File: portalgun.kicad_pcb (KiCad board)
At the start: 4 copper layers, 125.5 x 52.3 mm, 63 parts, among them J1 Conn_01x02_Male, J2 Rotary Encoder / Switch Header, J3 Conn_01x02_Male, J4 Conn_01x02_Male, J5 Conn_02x03_Odd_Even, J6 AVR-ISP-6, J7 Conn_01x04_Male, J8 Conn_01x04_Male, Q1 MMBT3904, Q2 MMBT3904, Q3 MMBT3904, Q4 MMBT3904, Q5 MMBT3904, U1 NCP1421, U2 LM358, U3 NCP4589DSN33T1G, U4 STM32L011G4Ux, U5 SC56-11GWA, U6 SC56-11GWA, U7 ATmega48P-20MMHR, U8 SC56-11GWA, U9 SC56-11GWA

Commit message: Main Board Rev A files
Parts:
- removed C12, C14: 1uF, Capacitor_SMD:C_0603_1608Metric
- removed J6: AVR-ISP-6, Connector_PinHeader_2.54mm:PinHeader_2x03_P2.54mm_Vertical
- removed J7, J8: Conn_01x04_Male, Connector_PinHeader_2.00mm:PinHeader_1x04_P2.00mm_Vertical
- removed Q4, Q5: MMBT3904, Package_TO_SOT_SMD:SOT-23
- removed R12, R31, R32, R33, R34: 100, Resistor_SMD:R_0603_1608Metric_Pad0.98x0.95mm_HandSolder
- removed R19, R20, R29, R30: 1k, Resistor_SMD:R_0603_1608Metric
- removed R21, R22, R23, R24, R25, R26, R27, R28: 220, Resistor_SMD:R_0603_1608Metric
- removed R7: 10k, Resistor_SMD:R_0603_1608Metric_Pad0.98x0.95mm_HandSolder
- removed U9: SC56-11GWA, Display_Kingbright:SC56-11GWA
- added C3: 1uF, Capacitor_SMD:C_0603_1608Metric, F.Cu at (203.2, 98.0)
- added C4: 100nF, Capacitor_SMD:C_0603_1608Metric, F.Cu at (201.7, 98.0)
- added C9: 1uF, Capacitor_SMD:C_0603_1608Metric, F.Cu at (216.2, 97.5)
- added J10: Conn_01x02_Male, Connector_PinHeader_2.00mm:PinHeader_1x02_P2.00mm_Vertical, F.Cu at (186.5, 116.0)
- added J9: Conn_01x04_Female, Connector_Molex:Molex_PicoBlade_53047-0410_1x04_P1.25mm_Vertical, F.Cu at (209.0, 95.0)
- added R15: 10k, Resistor_SMD:R_0603_1608Metric, F.Cu at (207.8, 100.8)
- added R16: 10k, Resistor_SMD:R_0603_1608Metric, F.Cu at (207.8, 103.9)
- added SW1: SW_MEC_5E, Button_Switch_THT:SW_TH_Tactile_Omron_B3F-10xx, F.Cu at (210.1, 116.1)
- added SW2: SW_MEC_5E, Button_Switch_THT:SW_TH_Tactile_Omron_B3F-10xx, F.Cu at (210.1, 106.2)
- C10, C8: value 10uF -> 1uF; footprint Capacitor_Tantalum_SMD:CP_EIA-2012-15_AVX-P -> Capacitor_SMD:C_0603_1608Metric
- C2: value 1uF -> 10uF; footprint Capacitor_SMD:C_0603_1608Metric -> Capacitor_SMD:C_0805_2012Metric; moved to F.Cu
- J2: value Rotary Encoder / Switch Header -> Conn_01x07_Male; footprint Connector_PinHeader_2.00mm:PinHeader_1x05_P2.00mm_Vertical -> Connector_Molex:Molex_PicoBlade_53047-0710_1x07_P1.25mm_Vertical
- J5: value Conn_02x03_Odd_Even -> Conn_01x02_Male; footprint Connector_PinHeader_2.54mm:PinHeader_1x06_P2.54mm_Horizontal -> Connector_PinHeader_2.00mm:PinHeader_1x02_P2.00mm_Vertical
- Q1: value MMBT3904 -> BS316N
- Q2, Q3: value MMBT3904 -> BS316N; moved to F.Cu
- R10, R11: value 100 -> 200; footprint Resistor_SMD:R_0603_1608Metric_Pad0.98x0.95mm_HandSolder -> Resistor_SMD:R_0603_1608Metric
- R5: value 10k -> 1k; footprint Resistor_SMD:R_0603_1608Metric_Pad0.98x0.95mm_HandSolder -> Resistor_SMD:R_0603_1608Metric
- R6: footprint Resistor_SMD:R_0603_1608Metric_Pad0.98x0.95mm_HandSolder -> Resistor_SMD:R_0603_1608Metric
- R8: value 1k -> 200; footprint Resistor_SMD:R_0603_1608Metric_Pad0.98x0.95mm_HandSolder -> Resistor_SMD:R_0603_1608Metric
- R9: value 100 -> 10k; footprint Resistor_SMD:R_0603_1608Metric_Pad0.98x0.95mm_HandSolder -> Resistor_SMD:R_0603_1608Metric
- U2: value LM358 -> ESP-12F; footprint Package_SO:SSOP-8_3.95x5.21x3.27mm_P1.27mm -> RF_Module:ESP-12E
- U3: value NCP4589DSN33T1G -> MIC5504-3.3YM5
- U4: value STM32L011G4Ux -> SGTL5000XNLA3; footprint Package_DFN_QFN:QFN-28_4x4mm_P0.5mm -> Package_DFN_QFN:QFN-20-1EP_3x3mm_P0.4mm_EP1.65x1.65mm
- U5: value SC56-11GWA -> MIC5504-1.8YM5; footprint Display_Kingbright:SC56-11GWA -> Package_TO_SOT_SMD:SOT-23-5
- U6, U8: value SC56-11GWA -> 74AHC1G125; footprint Display_Kingbright:SC56-11GWA -> Package_TO_SOT_SMD:SOT-353_SC-70-5
- U7: value ATmega48P-20MMHR -> 74AHC1G125; footprint Package_DFN_QFN:QFN-28-1EP_4x4mm_P0.45mm_EP2.4x2.4mm -> Package_TO_SOT_SMD:SOT-353_SC-70-5; moved to F.Cu
- moved U2 179.2 mm to (234.8, 112.9), turned to 180 degrees
- moved C11 176.7 mm to (239.8, 96.5), turned to 90 degrees
- moved C10 149.3 mm to (204.0, 106.7), turned to 270 degrees
- moved J4 140.8 mm to (204.5, 94.2), turned to 270 degrees
- moved C2 110.6 mm to (241.8, 96.5), turned to 90 degrees
- moved U8 103.7 mm to (223.8, 101.1), turned to 270 degrees
- moved U6 96.9 mm to (217.7, 101.1)
- moved U7 93.6 mm to (220.7, 101.1), turned to 90 degrees
- moved U5 82.7 mm to (201.2, 106.9), turned to 0 degrees
- moved Q3 69.4 mm to (199.8, 112.5)
- moved Q2 65.7 mm to (191.3, 112.5), turned to 270 degrees
- moved C1 54.8 mm to (185.2, 97.0), turned to 180 degrees
- moved J1 52.8 mm to (186.2, 94.2), turned to 270 degrees
- moved C7 47.1 mm to (187.5, 109.5), turned to 180 degrees
- moved L1 46.5 mm to (189.2, 98.6), turned to 270 degrees
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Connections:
- net Net-(U4-Pad4) renamed /Audio DAC/HP_L
- C10 pad 1: Net-(C10-Pad1) -> +1V8
- C10 pad 2: Net-(C10-Pad2) -> GND
- C11 pad 1: Net-(C11-Pad1) -> +3V3
- C11 pad 2: Net-(C11-Pad2) -> GND
- C2 pad 1: VBAT -> +3V3
- C8 pad 1: VBAT -> +3V3
- J2 pad 1: SWITCH -> +5V
- J2 pad 2: +3V3 -> GND
- J2 pad 3: ENCODER_B -> Net-(J2-Pad3)
- J2 pad 4: +3V3 -> Net-(J2-Pad4)
- J2 pad 5: ENCODER_A -> Net-(J2-Pad5)
- J3 pad 1: VBAT -> Net-(J3-Pad1)
- J4 pad 1: Net-(C11-Pad2) -> /Audio DAC/AOUT+
- J4 pad 2: GND -> /Audio DAC/AOUT-
- J5 pad 1: +3V3 -> Net-(J5-Pad1)
- Q1 pad 1: Net-(Q1-Pad1) -> LED1
- Q1 pad 3: Net-(J3-Pad2) -> Net-(J10-Pad2)
- Q2 pad 1: Net-(Q2-Pad1) -> LED2
- Q2 pad 3: Net-(Q2-Pad3) -> Net-(J5-Pad2)
- Q3 pad 1: Net-(Q3-Pad1) -> LED3
- Q3 pad 3: Net-(Q3-Pad3) -> Net-(J3-Pad2)
- R10 pad 1: Net-(J5-Pad3) -> Net-(J5-Pad1)
- R10 pad 2: LPUART1_TX -> +5V
- R11 pad 1: SYS_SWCLK -> Net-(J10-Pad1)
- R11 pad 2: Net-(J5-Pad4) -> +5V
- R5 pad 1: ENCODER_A -> Net-(J2-Pad5)
- R5 pad 2: GND -> Net-(R5-Pad2)
- R6 pad 1: ENCODER_B -> /bootsel
- R6 pad 2: GND -> +3V3
- R8 pad 1: LED_GATE -> Net-(J3-Pad1)
- R8 pad 2: Net-(Q1-Pad1) -> +5V
- R9 pad 1: SYS_SWDIO -> +3V3
- R9 pad 2: Net-(J5-Pad2) -> /~rst
- U2 pad 1: Net-(C11-Pad1) -> /~rst
- U2 pad 2: Net-(C11-Pad1) -> Net-(U2-Pad2)
- U2 pad 3: Net-(C10-Pad2) -> +3V3
- U2 pad 4: (no net) -> Net-(U2-Pad4)
- U2 pad 5: (no net) -> LED3
- U2 pad 6: (no net) -> LED2
- U2 pad 7: (no net) -> LED1
- U2 pad 8: (no net) -> +3V3
- U3 pad 4: +5V -> Net-(U3-Pad4)
- U4 pad 1: Net-(U4-Pad1) -> /Audio DAC/AOUT+
- U4 pad 11: SPI1_SCK -> Net-(U4-Pad11)
- U4 pad 12: SPI1_MISO -> +1V8
- U4 pad 13: SPI1_MOSI -> /Audio DAC/SYS_MCLK
- U4 pad 14: Net-(U4-Pad14) -> I2S_LRCLK
- U4 pad 15: Net-(U4-Pad15) -> I2S_BCLK
- U4 pad 16: GND -> /Audio DAC/I2S_DOUT
- U4 pad 17: +3V3 -> ESP_RXD
- U4 pad 18: SPI1_NSS -> SDA
- U4 pad 19: I2C1_SCL -> SCL
- U4 pad 2: Net-(U4-Pad2) -> /Audio DAC/AOUT-
- U4 pad 20: I2C1_SDA -> +3V3
- U4 pad 21: SYS_SWDIO -> GND
- U4 pad 3: Net-(U4-Pad3) -> +3V3
- U4 pad 5: +3V3 -> /Audio DAC/VAG
- U4 pad 6: LPUART1_RX -> Net-(U4-Pad6)
- U4 pad 7: LPUART1_TX -> Net-(U4-Pad7)
- U5 pad 1: /7 Segment Display/segment_g -> +3V3
- U5 pad 2: /7 Segment Display/segment_f -> GND
- U5 pad 3: Net-(U5-Pad3) -> +3V3
- U5 pad 4: /7 Segment Display/segment_a -> Net-(U5-Pad4)
- U5 pad 5: /7 Segment Display/segment_b -> +1V8
- U6 pad 1: /7 Segment Display/segment_g -> GND
- U6 pad 2: /7 Segment Display/segment_f -> SPI1_SCK
- U6 pad 3: Net-(U6-Pad3) -> GND
- U6 pad 4: /7 Segment Display/segment_a -> Net-(J2-Pad3)
- U6 pad 5: /7 Segment Display/segment_b -> +5V
- U7 pad 1: Net-(R24-Pad1) -> GND
- U7 pad 2: Net-(R25-Pad1) -> SPI1_MOSI
- U7 pad 3: VBAT -> GND
- U7 pad 4: GND -> Net-(J2-Pad4)
- U7 pad 5: Net-(U7-Pad5) -> +5V
- U8 pad 1: /7 Segment Display/segment_g -> GND
- U8 pad 2: /7 Segment Display/segment_f -> Net-(R5-Pad2)
- U8 pad 3: Net-(U8-Pad3) -> GND
- U8 pad 4: /7 Segment Display/segment_a -> SPI1_MISO
- U8 pad 5: /7 Segment Display/segment_b -> +5V
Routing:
- net LED1: track 0.00 -> 61.5 mm, vias 0 -> 2
- net /7 Segment Display/segment_g: track 56.9 -> 0.00 mm, vias 1 -> 0
- net /7 Segment Display/segment_b: track 55.0 -> 0.00 mm, vias 3 -> 0
- net LED2: track 0.00 -> 53.6 mm, vias 0 -> 2
- net /7 Segment Display/segment_f: track 53.5 -> 0.00 mm, vias 2 -> 0
- net /7 Segment Display/segment_e: track 51.3 -> 0.00 mm
- net /7 Segment Display/segment_a: track 48.3 -> 0.00 mm, vias 2 -> 0
- net /7 Segment Display/segment_c: track 48.1 -> 0.00 mm
- net +5V: track 12.2 -> 59.5 mm, vias 0 -> 11
- net /7 Segment Display/segment_d: track 45.6 -> 0.00 mm
- net /~rst: track 0.00 -> 45.6 mm
- net LED3: track 0.00 -> 45.2 mm, vias 0 -> 2
- net /7 Segment Display/decimal_point: track 45.2 -> 0.00 mm
- net ESP_RXD: track 0.00 -> 36.9 mm, vias 0 -> 1
- net SCL: track 0.00 -> 32.0 mm
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- added copper zone on In2.Cu, net +5V
- added copper zone on In2.Cu, net VBAT
- removed copper zone on In2.Cu, net GND
- removed copper zone on In1.Cu, net VBAT
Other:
- board size 125.5 x 52.3 mm -> 61.5 x 25 mm
- net class Default: clearance 0.2032 -> 0.1524
- rule trace_clearance: 0.2032 -> 0.1524
- rule via_min_size: 0.4 -> 0.6
- board text added: "3V"
- board text added: "G"
- board text added: "GND"
- board text added: "MISO"
- board text added: "MOSI"
- board text added: "Portal Gun Main Board rev A"
- board text added: "RX"
- board text added: "SCK"
- board text added: "TX"
- board text added: "~RST"
- board text added: "~SS"
- board text removed: "Display TODO - Power and Ground traces - Decoupling caps - SPI header"
- board text removed: "Stackup 1 (F.Cu): Signal + ground pour 2 (In1.Cu): Ground plane 3: (In2. Cu): Power plane 4: (B.Cu): Signal + ground pour"

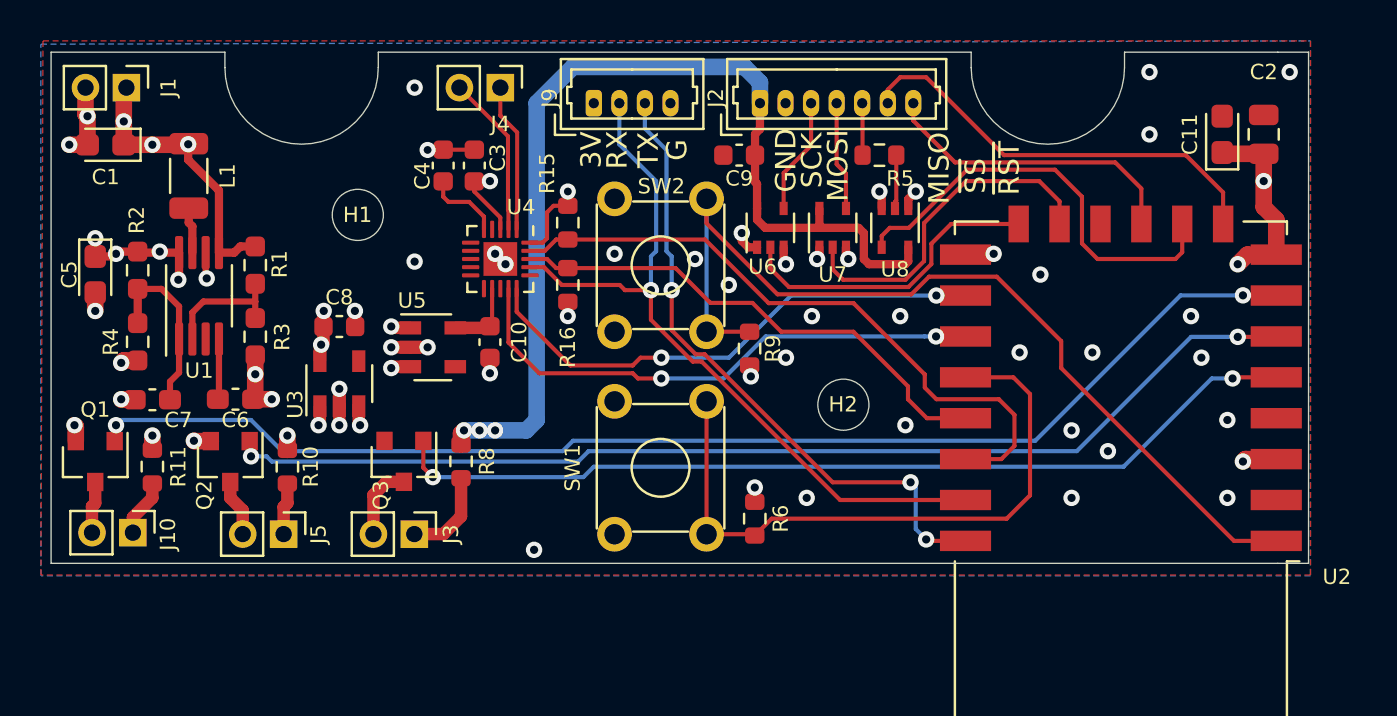
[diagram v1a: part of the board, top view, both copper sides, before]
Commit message: Rev B Portal Gun Mainboard as ordered
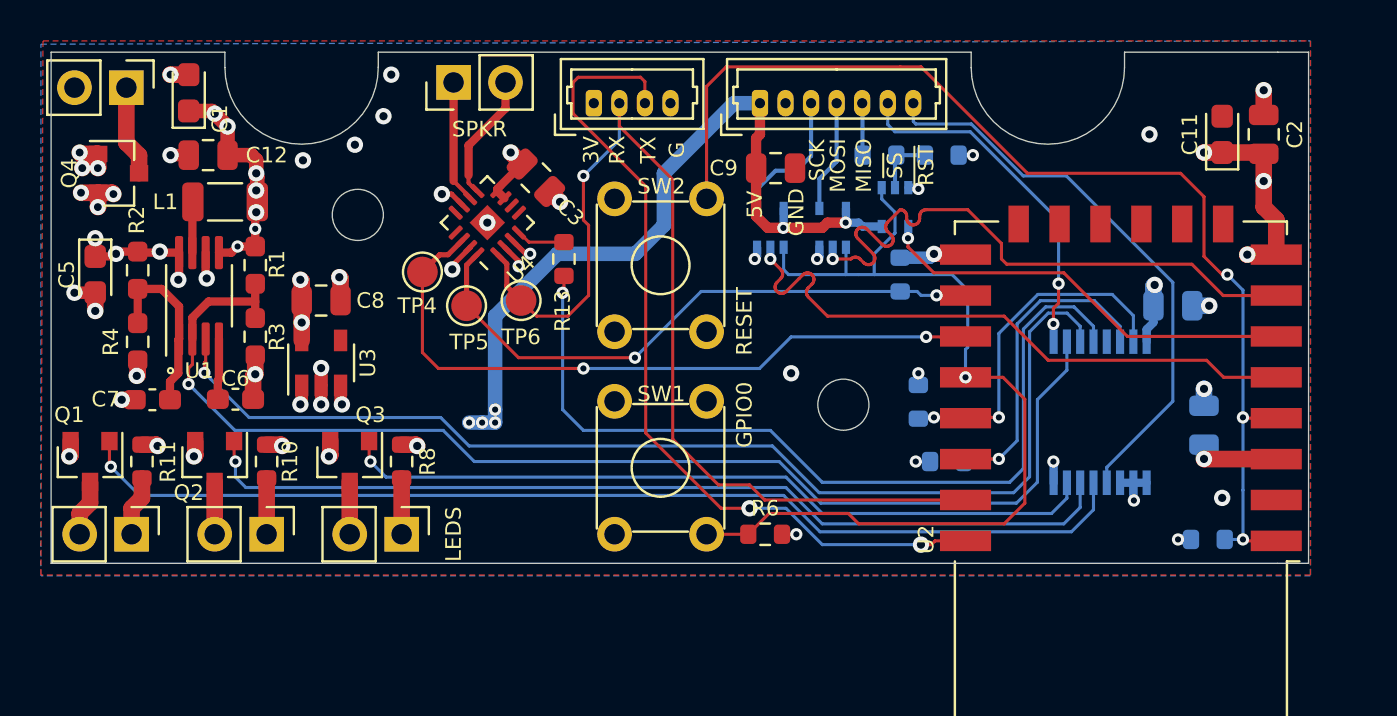
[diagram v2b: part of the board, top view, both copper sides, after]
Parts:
- removed C10: 1uF, Capacitor_SMD:C_0603_1608Metric
- removed C4: 100nF, Capacitor_SMD:C_0603_1608Metric
- removed U5: MIC5504-1.8YM5, Package_TO_SOT_SMD:SOT-23-5
- added C12: 1uF, Capacitor_SMD:C_0805_2012Metric, F.Cu at (190.2, 97.5)
- added C13: 1uF, Capacitor_SMD:C_0805_2012Metric, B.Cu at (238.9, 110.7)
- added C14: 1uF, Capacitor_SMD:C_0805_2012Metric, B.Cu at (237.4, 104.9)
- added Q4: Q_PMOS_DGS, Package_TO_SOT_SMD:SOT-23, F.Cu at (185.8, 98.4)
- added R12: 10k, Resistor_SMD:R_0603_1608Metric, B.Cu at (226.1, 97.5)
- added R13: 634kR, Resistor_SMD:R_0603_1608Metric, F.Cu at (207.6, 102.6)
- added R7: 10k, Resistor_SMD:R_0603_1608Metric, B.Cu at (224.0, 103.4)
- added TP4: I2S_LRCIN_TP, TestPoint:TestPoint_Pad_D1.5mm, F.Cu at (200.7, 103.3)
- added TP5: I2S_BCLK_TP, TestPoint:TestPoint_Pad_D1.5mm, F.Cu at (202.8, 104.9)
- added TP6: I2S_DIN_TP, TestPoint:TestPoint_Pad_D1.5mm, F.Cu at (205.5, 104.6)
- added U9: PCA9534, Package_SO:SSOP-16_5.3x6.2mm_P0.65mm, B.Cu at (233.8, 110.1)
- C2: value 10uF -> 1uF
- C3, C8, C9: footprint Capacitor_SMD:C_0603_1608Metric -> Capacitor_SMD:C_0805_2012Metric
- J1, J10, J3, J4, J5: footprint Connector_PinHeader_2.00mm:PinHeader_1x02_P2.00mm_Vertical -> Connector_PinHeader_2.54mm:PinHeader_1x02_P2.54mm_Vertical
- R15, R16, R5, R9, U6, U7, U8: moved to B.Cu
- U4: value SGTL5000XNLA3 -> MAX98357AETE; footprint Package_DFN_QFN:QFN-20-1EP_3x3mm_P0.4mm_EP1.65x1.65mm -> Package_DFN_QFN:TQFN-16-1EP_3x3mm_P0.5mm_EP1.23x1.23mm
- moved R9 24.3 mm to (239.1, 116.3), turned to 0 degrees
- moved R15 21.9 mm to (226.3, 112.5), turned to 0 degrees
- moved R16 18.1 mm to (224.9, 109.6), turned to 90 degrees
- moved C1 4.79 mm to (189.2, 94.5), turned to 90 degrees
- moved C3 3.07 mm to (206.2, 98.6), turned to 315 degrees
- moved R8 2.91 mm to (199.6, 112.5)
- moved Q3 2.65 mm to (197.1, 112.5)
- moved J4 2.30 mm to (202.2, 94.0), turned to 90 degrees
- moved L1 2.18 mm to (191.0, 99.8), turned to 180 degrees
- moved U4 1.89 mm to (203.8, 100.8), turned to 135 degrees
- moved C9 1.89 mm to (217.9, 98.2), turned to 0 degrees
- moved C8 1.55 mm to (195.7, 104.6)
- moved U3 1.35 mm to (195.7, 107.7)
- moved R10 1.05 mm to (193.0, 112.5)
- moved U8 1.02 mm to (223.8, 100.1)
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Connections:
- net /Audio DAC/SYS_MCLK renamed Net-(U4-Pad13)
- net LBI_EN renamed NCP_LBI_EN
- net Net-(J2-Pad3) renamed /EXT_SCK
- net Net-(J2-Pad4) renamed /EXT_MOSI
- net Net-(J2-Pad5) renamed /EXT_MISO
- J1 pad 1: VBAT -> /bat+
- J2 pad 6: SPI1_NSS -> ~SPI1_SS
- R6 pad 1: /bootsel -> ~BUFFER_EN
- SW1 pad 3: /bootsel -> ~BUFFER_EN
- SW1 pad 4: /bootsel -> Net-(SW1-Pad4)
- SW2 pad 3: /~rst -> Net-(SW2-Pad3)
- U1 pad 3: LBO -> NCP_LBO
- U2 pad 10: SPI1_MISO -> Net-(U2-Pad10)
- U2 pad 11: ~DISPLAY_RST -> Net-(U2-Pad11)
- U2 pad 13: SPI1_MOSI -> Net-(U2-Pad13)
- U2 pad 14: SPI1_SCK -> Net-(U2-Pad14)
- U2 pad 18: /bootsel -> ~BUFFER_EN
- U2 pad 4: Net-(U2-Pad4) -> /~rst
- U2 pad 5: LED3 -> SPI1_SCK
- U2 pad 6: LED2 -> SPI1_MISO
- U2 pad 7: LED1 -> SPI1_MOSI
- U2 pad 9: SPI1_NSS -> Net-(U2-Pad9)
- U4 pad 1: /Audio DAC/AOUT+ -> ESP_RXD
- U4 pad 10: Net-(U4-Pad10) -> /Audio DAC/AOUT+
- U4 pad 11: Net-(U4-Pad11) -> GND
- U4 pad 12: +1V8 -> Net-(U4-Pad12)
- U4 pad 15: I2S_BCLK -> GND
- U4 pad 16: /Audio DAC/I2S_DOUT -> I2S_BCLK
- U4 pad 17: ESP_RXD -> GND
- U4 pad 2: /Audio DAC/AOUT- -> +3V3
- U4 pad 3: +3V3 -> GND
- U4 pad 4: /Audio DAC/HP_L -> /Audio DAC/~SD_MODE
- U4 pad 5: /Audio DAC/VAG -> Net-(U4-Pad5)
- U4 pad 7: Net-(U4-Pad7) -> +3V3
- U4 pad 8: Net-(U4-Pad8) -> +3V3
- U4 pad 9: Net-(U4-Pad9) -> /Audio DAC/AOUT-
- U6 pad 1: GND -> ~BUFFER_EN
- U7 pad 1: GND -> ~BUFFER_EN
- U8 pad 1: GND -> ~BUFFER_EN
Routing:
- net NCP_LBO: track 0.00 -> 55.8 mm, vias 0 -> 1
- net NCP_LBI_EN: track 6.27 -> 61.9 mm, vias 0 -> 1
- net ~BUFFER_EN: track 0.00 -> 46.1 mm, vias 0 -> 1
- net /Audio DAC/~SHUTDOWN: track 0.00 -> 42.7 mm, vias 0 -> 1
- net /bootsel: track 31.6 -> 0.00 mm
- net SPI1_NSS: track 21.2 -> 0.00 mm
- net ~SPI1_SS: track 0.00 -> 17.4 mm, vias 0 -> 2
- net SPI1_SCK: track 15.4 -> 30.5 mm, vias 0 -> 1
- net SCL: track 32.0 -> 17.2 mm, vias 0 -> 1
- net SPI1_MOSI: track 17.0 -> 30.5 mm, vias 0 -> 1
- net ESP_RXD: track 36.9 -> 50.1 mm
- net ~DISPLAY_RST: track 15.1 -> 28.0 mm
- net ESP_TXD: track 31.5 -> 41.4 mm, vias 3 -> 2
- net /~rst: track 45.6 -> 54.8 mm, vias 0 -> 3
- net LED1: track 61.5 -> 52.4 mm, vias 2 -> 1
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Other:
- net class Default: trace_width 0.2032 -> 0.1524; via_dia 0.7874 -> 0.6; via_drill 0.381 -> 0.3
- net class Finepitch: via_dia 0.7874 -> 0.6; via_drill 0.381 -> 0.3
- board text added: "+"
- board text added: "5V"
- board text added: "GPIO0"
- board text added: "LEDS"
- board text added: "Portal Gun Main Board rev B For Jasmine <3"
- board text added: "RESET"
- board text added: "SPKR"
- board text removed: "Portal Gun Main Board rev A"

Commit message: Updates. Firmware running on main board rev B
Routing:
- net ~DISPLAY_RST: track 28.0 -> 27.5 mm
